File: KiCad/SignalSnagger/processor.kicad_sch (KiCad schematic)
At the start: 80 parts, among them J201 Conn_01x01_Female, J202 Conn_01x01_Female, J203 Conn_01x02, J204 Conn_01x02, J205 Conn_01x01_Female, J206 Conn_01x01_Female, J207 Conn_01x01_Female, J210 Conn_01x01_Female, J211 Conn_01x01_Female, J212 Conn_01x01_Female, J213 Conn_01x01_Female, J214 Conn_01x01_Female, J215 Conn_01x01_Female, J216 Conn_01x01_Female, J217 Conn_01x01_Female, J218 Conn_01x02, J219 Conn_01x02, P201 ISP/PDI, Q201 BSS84W-7-F, Q202 BSS138W-7-F, SW201 SW_SPST, SW202 SW_SPST, SW203 PEC12R-4225F-S0024, U201 AVR128DA48, U202 SI5351, U206 LP2985-5.0, U207 MAX1683EUK, X202 25 MHz, X901 ECS-327TXO-30-TR

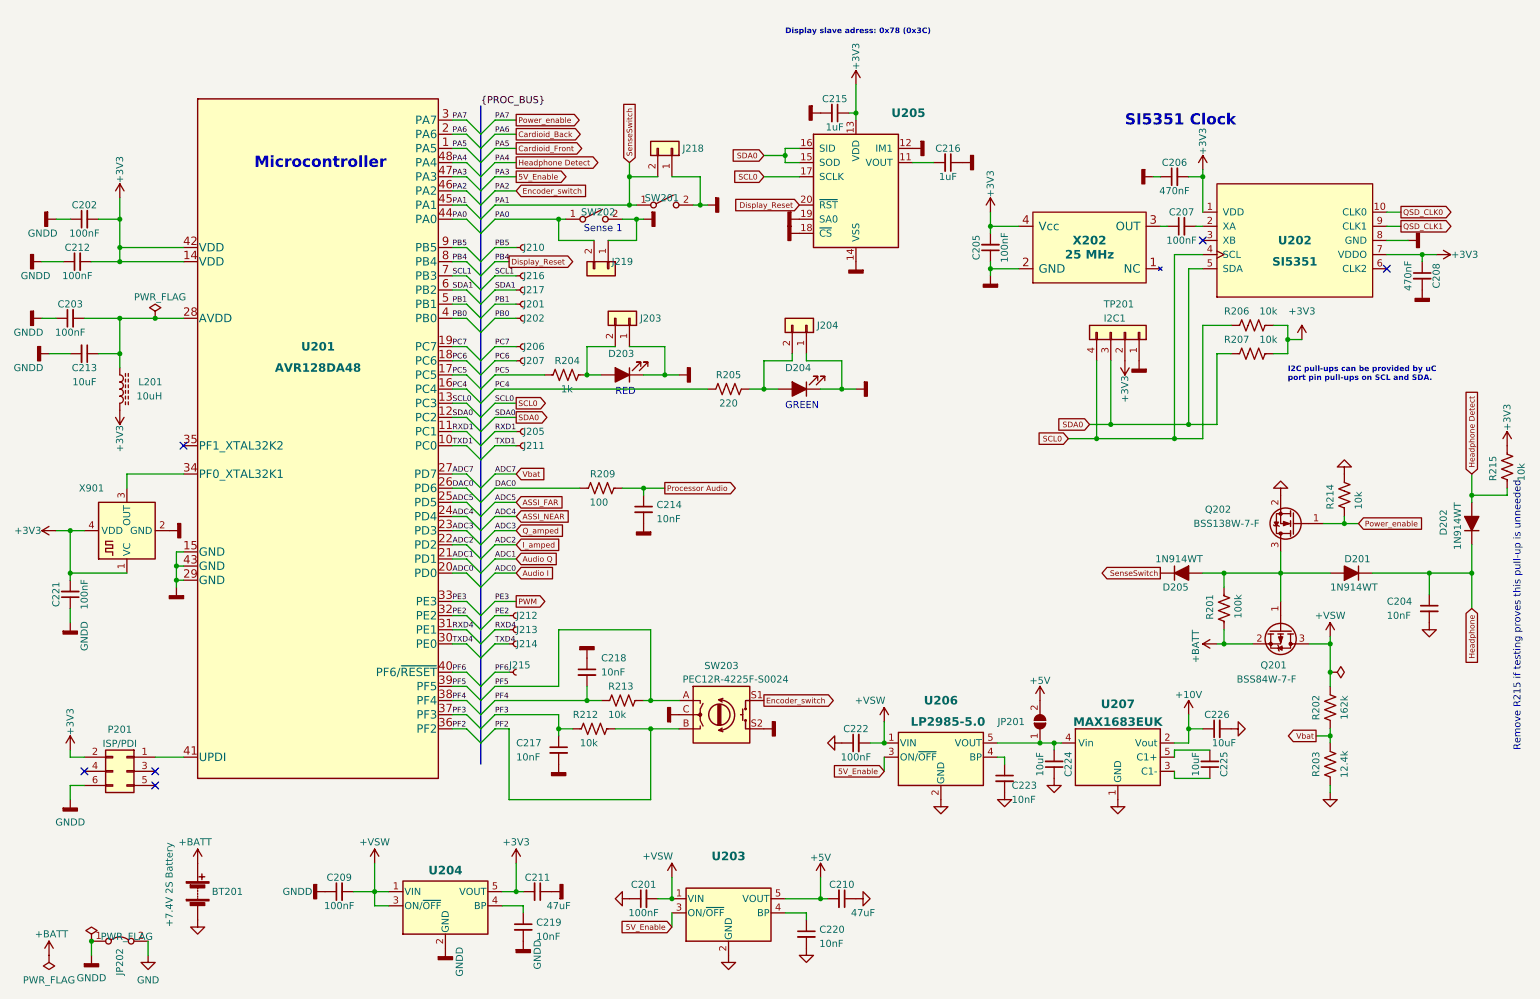
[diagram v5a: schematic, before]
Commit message: Schematic PDF File
Updated date on schematic and printed an updated PDF schematic. No changes made to design.
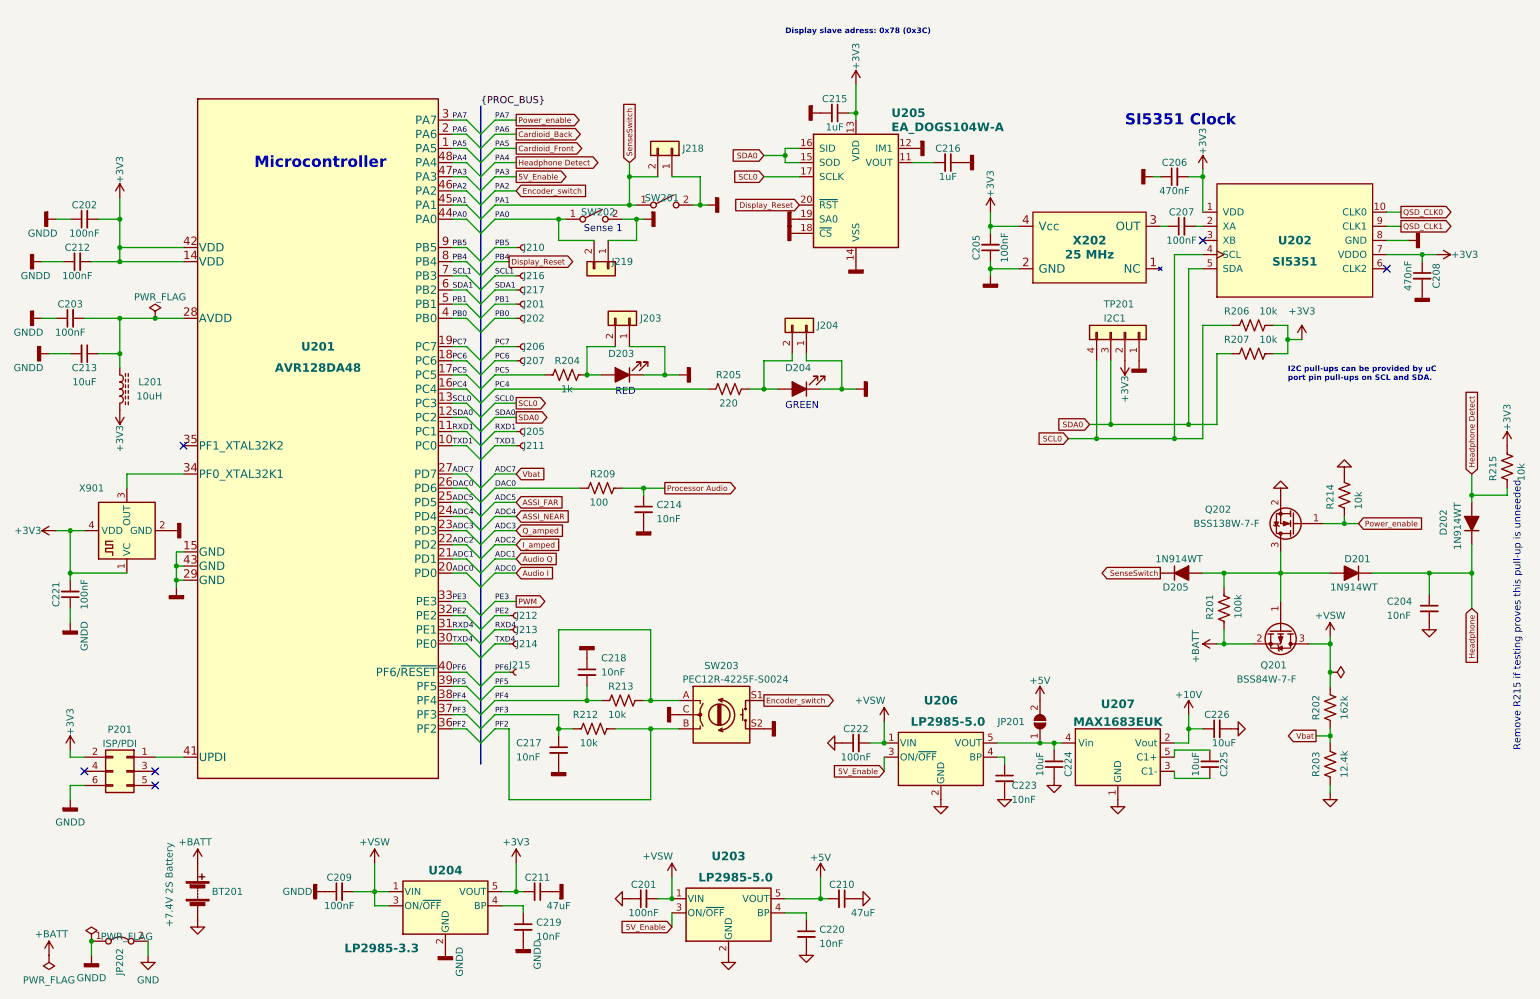
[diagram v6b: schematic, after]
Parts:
- U203: value (none) -> LP2985-5.0; footprint (none) -> Package_TO_SOT_SMD:SOT-23-5
- U204: value (none) -> LP2985-3.3; footprint (none) -> Package_TO_SOT_SMD:SOT-23-5
- U205: value (none) -> EA_DOGS104W-A; footprint (none) -> Display:EA_DOGS104X-A
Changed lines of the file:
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@@
   (title_block
     (title "SignalSnagger")
-    (date "2024-04-13")
+    (date "2024-05-03")
     (rev "0.317")
   )
@@
       (effects (font (size 1.54 1.54) bold) (justify left))
     )
-    (property "Value" "" (id 1) (at 170.18 41.91 0)
+    (property "Value" "EA_DOGS104W-A" (id 1) (at 170.18 41.91 0)
       (effects (font (size 1.54 1.54) bold) (justify left))
     )
-    (property "Footprint" "" (id 2) (at 163.83 68.58 0)
+    (property "Footprint" "Display:EA_DOGS104X-A" (id 2) (at 163.83 68.58 0)
       (effects (font (size 1.27 1.27)) hide)
     )
@@
       (effects (font (size 1.54 1.54) bold))
     )
-    (property "Value" "" (id 1) (at 142.24 176.53 0)
+    (property "Value" "LP2985-5.0" (id 1) (at 142.24 176.53 0)
       (effects (font (size 1.54 1.54) bold))
     )
-    (property "Footprint" "" (id 2) (at 140.97 174.625 0)
+    (property "Footprint" "Package_TO_SOT_SMD:SOT-23-5" (id 2) (at 140.97 174.625 0)
       (effects (font (size 1.27 1.27)) hide)
     )
@@
       (effects (font (size 1.54 1.54) bold))
     )
-    (property "Value" "" (id 1) (at 78.74 189.23 0)
+    (property "Value" "LP2985-3.3" (id 1) (at 78.74 189.23 0)
       (effects (font (size 1.54 1.54) bold))
     )
-    (property "Footprint" "" (id 2) (at 90.17 173.355 0)
+    (property "Footprint" "Package_TO_SOT_SMD:SOT-23-5" (id 2) (at 90.17 173.355 0)
       (effects (font (size 1.27 1.27)) hide)
     )

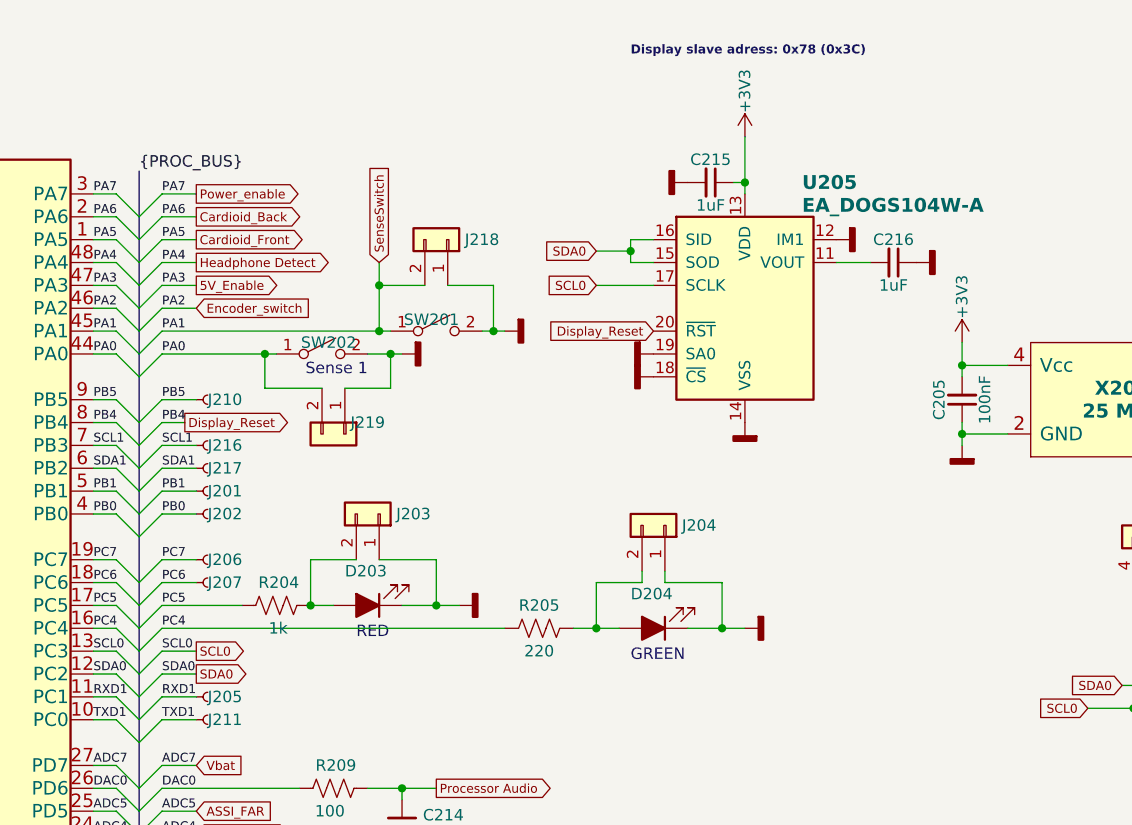
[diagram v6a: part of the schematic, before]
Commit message: Updated Schematic
o Updated T101 to accept Coilcraft part
o Added J208 to support an external I2C module
o Added D206 to block battery voltage
o Updated PCB with changes above
o Corrected silkscreen
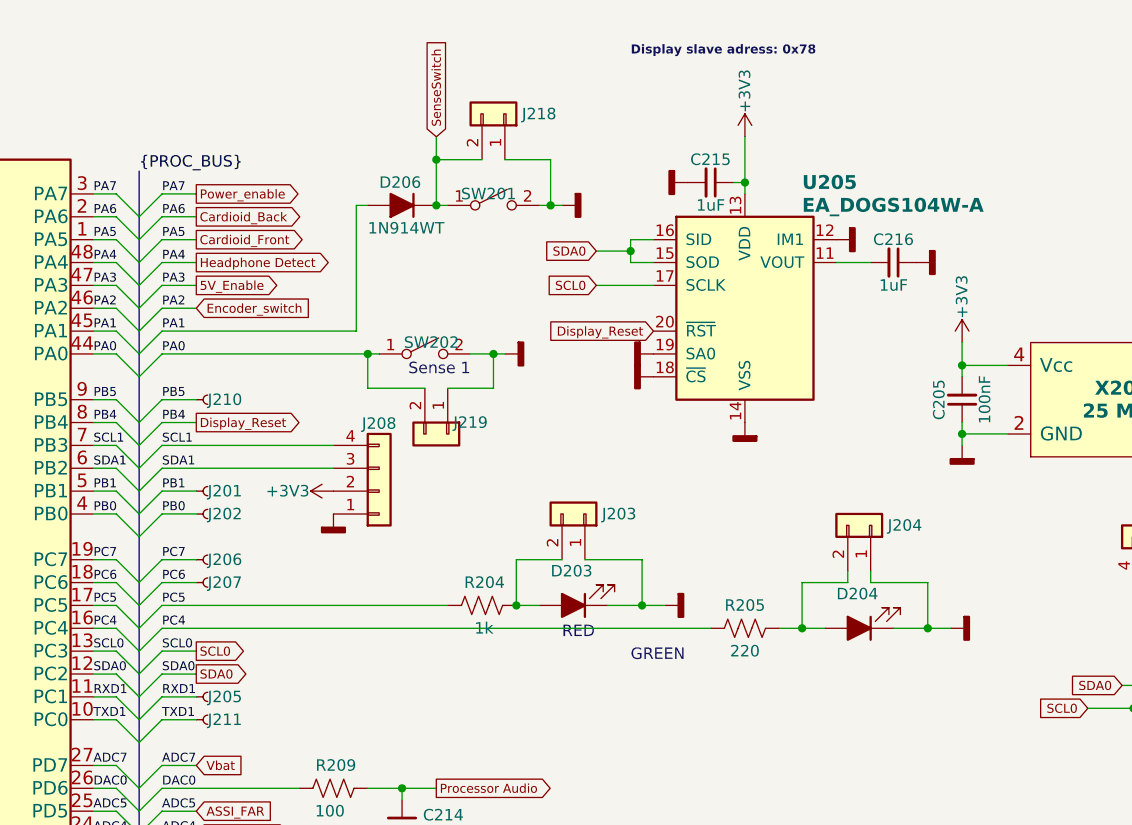
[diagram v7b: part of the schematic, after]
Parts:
- removed J216, J217: Conn_01x01_Female, Oddities:Dummy_Empty, symbol Connector:Conn_01x01_Generic
- added D206: 1N914WT, Diode_SMD:D_SOD-523, symbol Diode:1N914WT
- added J208: Conn_01x04, Connector_PinHeader_1.27mm:PinHeader_1x04_P1.27mm_Vertical, symbol Connector_Generic:Conn_01x04
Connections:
- net +3V3: now also J208.2 (Pin_2)
- net GNDD: now also J208.1 (Pin_1)
- net SCL1: now also J208.4 (Pin_4)
- net SDA1: now also J208.3 (Pin_3)
- net SenseSwitch: now also D206.1 (K); no longer U201.45 (PA1)
- new net PA1: D206.2 (A), U201.45 (PA1)
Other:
- note added: "Display slave adress: 0x78"
- note removed: "Display slave adress: 0x78 (0x3C)"
- moved on the sheet: D203, D204, J203, J204, J218, J219, R204, R205, SW201, SW202

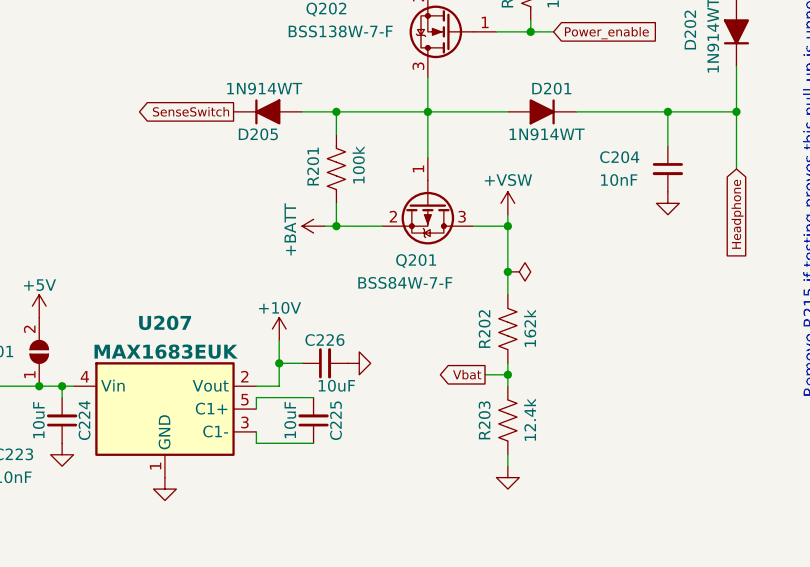
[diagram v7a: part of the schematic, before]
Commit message: Schematic and PCB Updates
o Changed power rating of R320 and R909
o Changed Q201 to a 1-Amp part
o Updated Gerbers
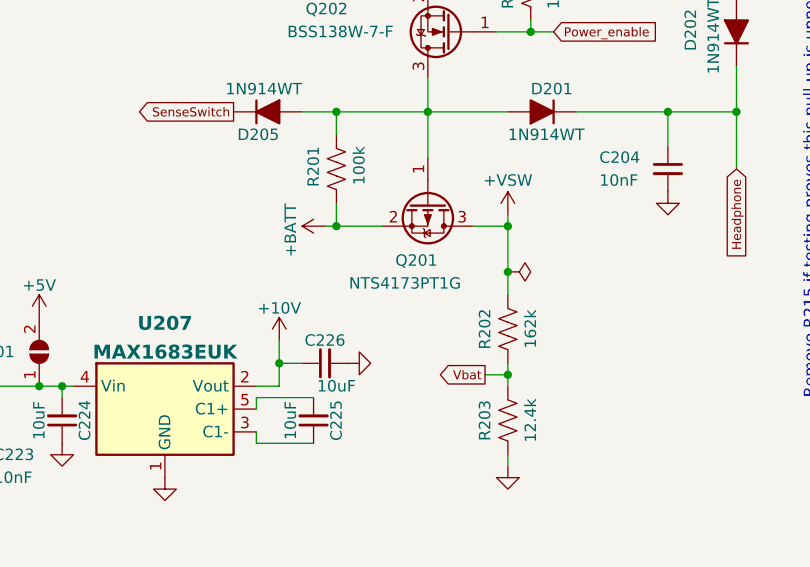
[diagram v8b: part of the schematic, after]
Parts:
- Q201: value BSS84W-7-F -> NTS4173PT1G; Digi-Key Part No. BSS84W-FDICT-ND -> NTS4173PT1GOSCT-ND; LCSC Part Number C110490 -> (none); Link https://www.digikey.com/short/fjvhfm07 -> https://www.digikey.com/short/vpmddfwp; Manufacturer Diodes Incorporated -> Onsemi; Manufacturer PN BSS84W-7-F -> NTS4173PT1G
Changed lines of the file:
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@@
     (in_bom yes) (on_board yes)
     (property "Reference" "Q201" (id 0) (at 238.76 138.43 90))
-    (property "Value" "BSS84W-7-F" (id 1) (at 237.49 140.97 90))
+    (property "Value" "NTS4173PT1G" (id 1) (at 237.49 140.97 90))
     (property "Footprint" "Package_TO_SOT_SMD:SOT-323_SC-70" (id 2) (at 238.125 137.16 0)
       (effects (font (size 1.27 1.27) italic) (justify left) hide)
@@
       (effects (font (size 1.27 1.27)) (justify left) hide)
     )
-    (property "Digi-Key Part No." "BSS84W-FDICT-ND" (id 4) (at 240.03 132.08 0)
+    (property "Digi-Key Part No." "NTS4173PT1GOSCT-ND" (id 4) (at 240.03 132.08 0)
       (effects (font (size 1.27 1.27)) hide)
     )
-    (property "Manufacturer" "Diodes Incorporated" (id 5) (at 240.03 132.08 0)
+    (property "Manufacturer" "Onsemi" (id 5) (at 240.03 132.08 0)
       (effects (font (size 1.27 1.27)) hide)
     )
-    (property "Manufacturer PN" "BSS84W-7-F" (id 6) (at 240.03 132.08 0)
+    (property "Manufacturer PN" "NTS4173PT1G" (id 6) (at 240.03 132.08 0)
       (effects (font (size 1.27 1.27)) hide)
     )
-    (property "Description" "MOSFET P-CH 50V 130MA SOT323" (id 7) (at 240.03 132.08 0)
+    (property "Description" "MOSFET P-CH 30V 1.2A SC70-3" (id 7) (at 240.03 132.08 0)
       (effects (font (size 1.27 1.27)) hide)
     )
-    (property "Link" "https://www.digikey.com/short/fjvhfm07" (id 8) (at 240.03 132.08 0)
+    (property "Link" "https://www.digikey.com/short/vpmddfwp" (id 8) (at 240.03 132.08 0)
       (effects (font (size 1.27 1.27)) hide)
     )
-    (property "LCSC Part Number" "C110490" (id 9) (at 240.03 132.08 0)
-      (effects (font (size 1.27 1.27)) hide)
-    )
